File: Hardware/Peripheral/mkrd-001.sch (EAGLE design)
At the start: 5 parts

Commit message: First try.
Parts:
- removed S1, S2: (no value), switch-dil:A1353HEX
- added J1: MKR, SparkFun-Connectors:CONN_05JST
- JP1: value (none) -> DISP; device pinhead:PINHD-2X8 -> SparkFun-Connectors:CONN_04
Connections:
- removed net ANLG0: JP1.3, S2.1
- removed net ANLG1: JP1.7, S2.4
- removed net ANLG2: JP1.11, S2.8
- removed net ANLG3: JP1.15, S2.2
- removed net DTCT0: JP1.2, S1.1
- removed net DTCT1: JP1.6, S1.4
- removed net DTCT2: JP1.10, S1.8
- removed net DTCT3: JP1.14, S1.2
- new net SCL: J1.3, JP1.3
- new net SDA: J1.2, JP1.4
- net GND: now also J1.1; no longer JP1.13, JP1.5, JP1.9, S1.C
- net VCC: now also J1.5, JP1.2; no longer JP1.12, JP1.16, JP1.4, JP1.8, S2.C
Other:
- note removed: "GeekPort II 1: GND 2: DTCT0 3: ANLG0 4: Vcc/2"
- note removed: "Pineapple -> Switch 1->1 2->4 4->8 8->2"

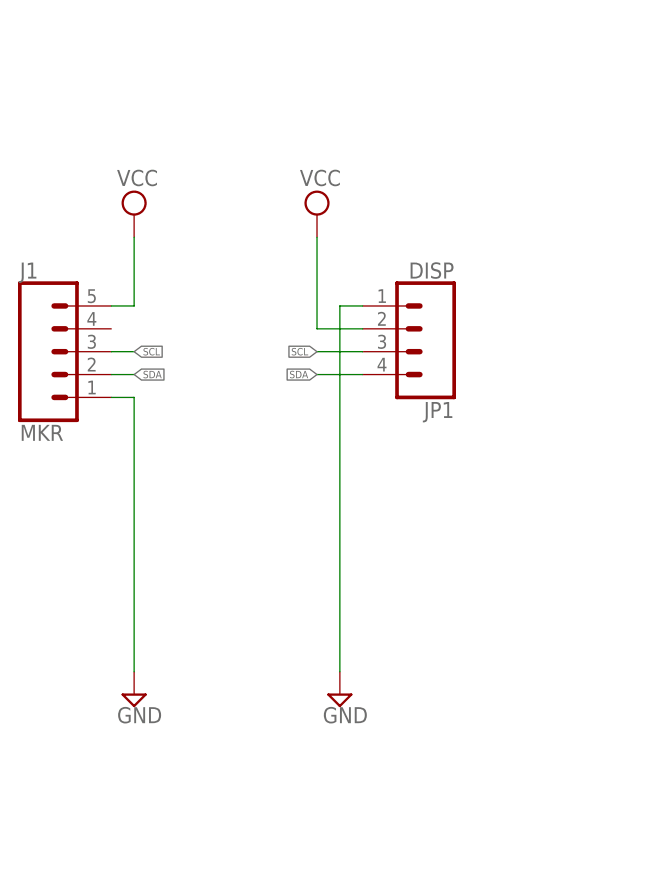
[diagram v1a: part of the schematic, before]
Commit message: Added cap.
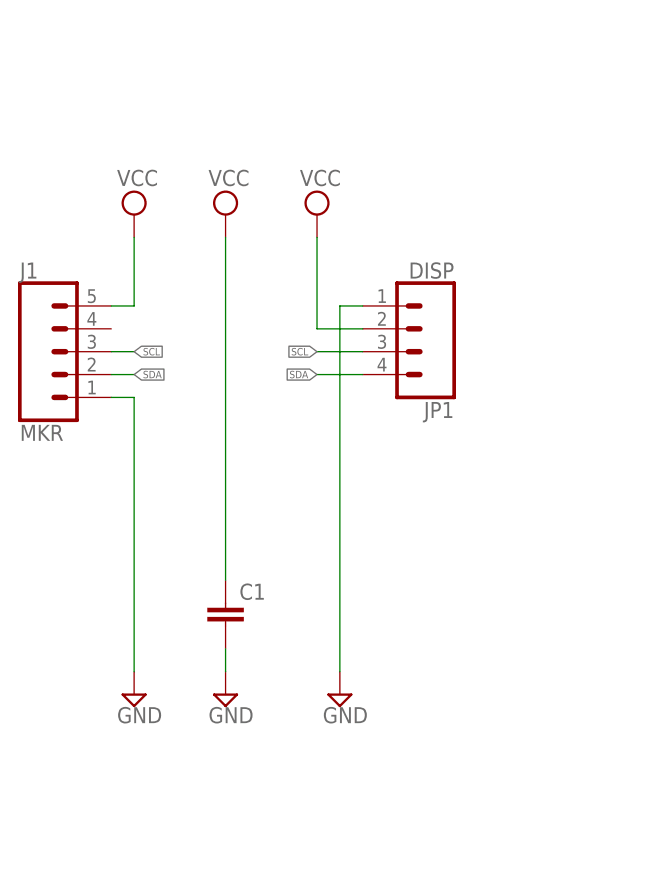
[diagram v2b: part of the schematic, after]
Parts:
- added C1: (no value), rcl:C-EU025-024X044
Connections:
- net GND: now also C1.2
- net VCC: now also C1.1
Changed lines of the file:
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@@
 <part name="SUPPLY2" library="supply2" library_urn="urn:adsk.eagle:library:372" deviceset="GND" device=""/>
 <part name="SUPPLY4" library="supply2" library_urn="urn:adsk.eagle:library:372" deviceset="VCC" device=""/>
+<part name="SUPPLY5" library="supply2" library_urn="urn:adsk.eagle:library:372" deviceset="GND" device=""/>
+<part name="SUPPLY6" library="supply2" library_urn="urn:adsk.eagle:library:372" deviceset="VCC" device=""/>
+<part name="C1" library="rcl" library_urn="urn:adsk.eagle:library:334" deviceset="C-EU" device="025-024X044" package3d_urn="urn:adsk.eagle:package:23630/1"/>
 </parts>
 <sheets>
@@
 <attribute name="VALUE" x="41.275" y="130.175" size="1.778" layer="96"/>
 </instance>
+<instance part="SUPPLY5" gate="GND" x="53.34" y="73.66" smashed="yes">
+<attribute name="VALUE" x="51.435" y="70.485" size="1.778" layer="96"/>
+</instance>
+<instance part="SUPPLY6" gate="G$1" x="53.34" y="127" smashed="yes">
+<attribute name="VALUE" x="51.435" y="130.175" size="1.778" layer="96"/>
+</instance>
+<instance part="C1" gate="G$1" x="53.34" y="83.82" smashed="yes">
+<attribute name="NAME" x="54.864" y="84.201" size="1.778" layer="95"/>
+<attribute name="VALUE" x="54.864" y="79.121" size="1.778" layer="96"/>
+</instance>
 </instances>
 <busses>
@@
 <pinref part="SUPPLY4" gate="G$1" pin="VCC"/>
 </segment>
+<segment>
+<pinref part="SUPPLY6" gate="G$1" pin="VCC"/>
+<pinref part="C1" gate="G$1" pin="1"/>
+<wire x1="53.34" y1="124.46" x2="53.34" y2="86.36" width="0.1524" layer="91"/>
+</segment>
 </net>
 <net name="GND" class="0">
@@
 <wire x1="43.18" y1="106.68" x2="43.18" y2="76.2" width="0.1524" layer="91"/>
 <pinref part="SUPPLY2" gate="GND" pin="GND"/>
+</segment>
+<segment>
+<pinref part="C1" gate="G$1" pin="2"/>
+<pinref part="SUPPLY5" gate="GND" pin="GND"/>
+<wire x1="53.34" y1="78.74" x2="53.34" y2="76.2" width="0.1524" layer="91"/>
 </segment>
 </net>
@@
 packages will not be understood (or retained) with this version.
 </note>
+<note version="8.4" severity="warning">
+Since Version 8.4, EAGLE supports properties for SPICE simulation.
+Probes in schematics and SPICE mapping objects found in parts and library devices
+will not be understood with this version. Update EAGLE to the latest version
+for full support of SPICE simulation.
+</note>
 </compatibility>

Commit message: Added new board.
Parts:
- removed JP1: DISP, SparkFun-Connectors:CONN_04
- added C2, C3: 1u, rcl:C-EU025-025X050
- added R1: 1.5k, rcl:R-EU_0204/5
- added R2: 3.3k, rcl:R-EU_0204/5
- added R3, R4: 10k, rcl:R-EU_0204/5
- added X1: AQM0802A-RN-GBW, AQM0802A-RN-GBW:AQM0802A-RN-GBW
- C1: value (none) -> 0.1u
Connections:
- new net 3V3: C1.1, C2.1, R1.2, R2.2, R3.1, R4.1, X1.5, X1.9
- new net N$1: C2.2, X1.2
- new net N$2: C3.2, X1.4
- new net N$3: C3.1, X1.3
- net GND: now also R2.1, X1.6; no longer JP1.1
- net SCL: now also R3.2, X1.8; no longer JP1.3
- net SDA: now also R4.2, X1.7; no longer JP1.4
- net VCC: now also R1.1; no longer C1.1, JP1.2
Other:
- moved on the sheet: C1

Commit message: Signal name.
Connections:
- net N$1 renamed LCDVOUT
- net N$2 renamed CAP1P
- net N$3 renamed CAP1N
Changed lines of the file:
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@@
 </segment>
 </net>
-<net name="N$2" class="0">
+<net name="CAP1P" class="0">
 <segment>
 <pinref part="X1" gate="G$1" pin="4"/>
@@
 </segment>
 </net>
-<net name="N$3" class="0">
+<net name="CAP1N" class="0">
 <segment>
 <pinref part="C3" gate="G$1" pin="1"/>
@@
 </segment>
 </net>
-<net name="N$1" class="0">
+<net name="LCDVOUT" class="0">
 <segment>
 <pinref part="X1" gate="G$1" pin="2"/>

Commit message: Silk.
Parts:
- renumbered X1 to LCD1
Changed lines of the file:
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@@
 <part name="SUPPLY5" library="supply2" library_urn="urn:adsk.eagle:library:372" deviceset="GND" device=""/>
 <part name="C1" library="rcl" library_urn="urn:adsk.eagle:library:334" deviceset="C-EU" device="025-024X044" package3d_urn="urn:adsk.eagle:package:23630/1" value="0.1u"/>
-<part name="X1" library="AQM0802A-RN-GBW" deviceset="AQM0802A-RN-GBW" device=""/>
+<part name="LCD1" library="AQM0802A-RN-GBW" deviceset="AQM0802A-RN-GBW" device=""/>
 <part name="R1" library="rcl" library_urn="urn:adsk.eagle:library:334" deviceset="R-EU_" device="0204/5" package3d_urn="urn:adsk.eagle:package:23488/1" value="1.5k"/>
 <part name="R2" library="rcl" library_urn="urn:adsk.eagle:library:334" deviceset="R-EU_" device="0204/5" package3d_urn="urn:adsk.eagle:package:23488/1" value="3.3k"/>
@@
 <attribute name="VALUE" x="59.944" y="79.121" size="1.778" layer="96"/>
 </instance>
-<instance part="X1" gate="G$1" x="119.38" y="114.3" smashed="yes">
+<instance part="LCD1" gate="G$1" x="119.38" y="114.3" smashed="yes">
 <attribute name="NAME" x="121.92" y="124.46" size="1.778" layer="95"/>
 <attribute name="VALUE" x="121.92" y="101.6" size="1.778" layer="96"/>
@@
 </segment>
 <segment>
-<pinref part="X1" gate="G$1" pin="6"/>
+<pinref part="LCD1" gate="G$1" pin="6"/>
 <wire x1="116.84" y1="111.76" x2="114.3" y2="111.76" width="0.1524" layer="91"/>
 <pinref part="SUPPLY3" gate="GND" pin="GND"/>
@@
 <wire x1="81.28" y1="111.76" x2="99.06" y2="111.76" width="0.1524" layer="91"/>
 <junction x="81.28" y="111.76"/>
-<pinref part="X1" gate="G$1" pin="8"/>
+<pinref part="LCD1" gate="G$1" pin="8"/>
 <wire x1="99.06" y1="111.76" x2="99.06" y2="106.68" width="0.1524" layer="91"/>
 <wire x1="99.06" y1="106.68" x2="116.84" y2="106.68" width="0.1524" layer="91"/>
@@
 <wire x1="96.52" y1="114.3" x2="96.52" y2="109.22" width="0.1524" layer="91"/>
 <wire x1="96.52" y1="109.22" x2="40.64" y2="109.22" width="0.1524" layer="91"/>
-<pinref part="X1" gate="G$1" pin="7"/>
+<pinref part="LCD1" gate="G$1" pin="7"/>
 <wire x1="116.84" y1="109.22" x2="96.52" y2="109.22" width="0.1524" layer="91"/>
 <junction x="96.52" y="109.22"/>
@@
 <junction x="66.04" y="114.3"/>
 <label x="60.96" y="116.84" size="1.778" layer="95"/>
-<pinref part="X1" gate="G$1" pin="9"/>
+<pinref part="LCD1" gate="G$1" pin="9"/>
 <wire x1="116.84" y1="104.14" x2="66.04" y2="104.14" width="0.1524" layer="91"/>
 <junction x="66.04" y="104.14"/>
@@
 <wire x1="58.42" y1="121.92" x2="99.06" y2="121.92" width="0.1524" layer="91"/>
 <wire x1="99.06" y1="121.92" x2="99.06" y2="114.3" width="0.1524" layer="91"/>
-<pinref part="X1" gate="G$1" pin="5"/>
+<pinref part="LCD1" gate="G$1" pin="5"/>
 <wire x1="99.06" y1="114.3" x2="116.84" y2="114.3" width="0.1524" layer="91"/>
 <pinref part="C2" gate="G$1" pin="1"/>
@@
 <net name="CAP1P" class="0">
 <segment>
-<pinref part="X1" gate="G$1" pin="4"/>
+<pinref part="LCD1" gate="G$1" pin="4"/>
 <pinref part="C3" gate="G$1" pin="2"/>
 <wire x1="104.14" y1="119.38" x2="104.14" y2="116.84" width="0.1524" layer="91"/>
@@
 <wire x1="104.14" y1="129.54" x2="106.68" y2="129.54" width="0.1524" layer="91"/>
 <wire x1="106.68" y1="129.54" x2="106.68" y2="119.38" width="0.1524" layer="91"/>
-<pinref part="X1" gate="G$1" pin="3"/>
+<pinref part="LCD1" gate="G$1" pin="3"/>
 <wire x1="106.68" y1="119.38" x2="116.84" y2="119.38" width="0.1524" layer="91"/>
 </segment>
@@
 <net name="LCDVOUT" class="0">
 <segment>
-<pinref part="X1" gate="G$1" pin="2"/>
+<pinref part="LCD1" gate="G$1" pin="2"/>
 <wire x1="116.84" y1="121.92" x2="114.3" y2="121.92" width="0.1524" layer="91"/>
 <pinref part="C2" gate="G$1" pin="2"/>
